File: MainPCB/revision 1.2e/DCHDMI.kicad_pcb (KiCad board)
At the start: 4 copper layers, 66.6 x 51.3 mm, 108 parts, among them CON1 3-1775333-2, CON2 2001-1-2-21-00-BK, U1 MCP1826S-1202E/DB, U2 MIC5219-2.5YM5-TR, U3 LP5907MFX-1.8/NOPB, U4 ADV7513, U5 664G-03LF, U6 10CL025, U7 MX25L1606EM1I-12G, U8 ESP-12E

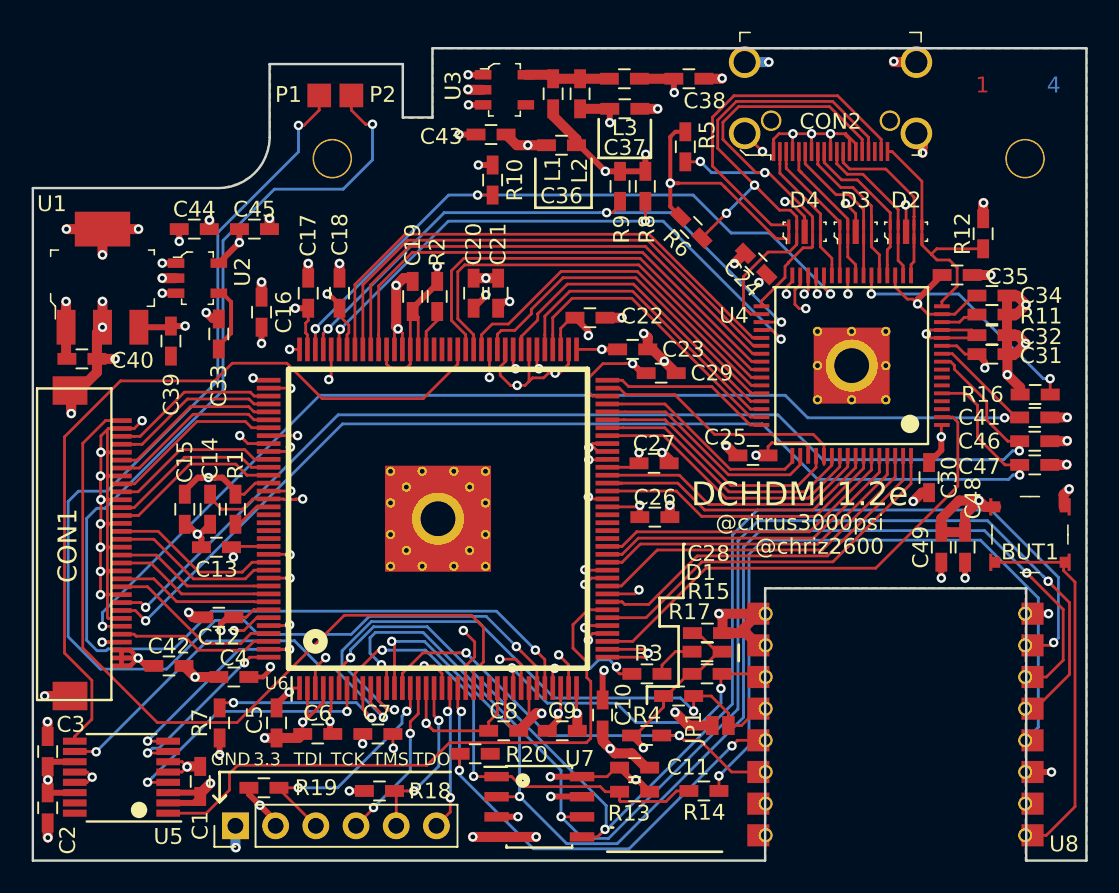
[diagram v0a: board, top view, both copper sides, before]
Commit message: Minor Update to Edge Cuts
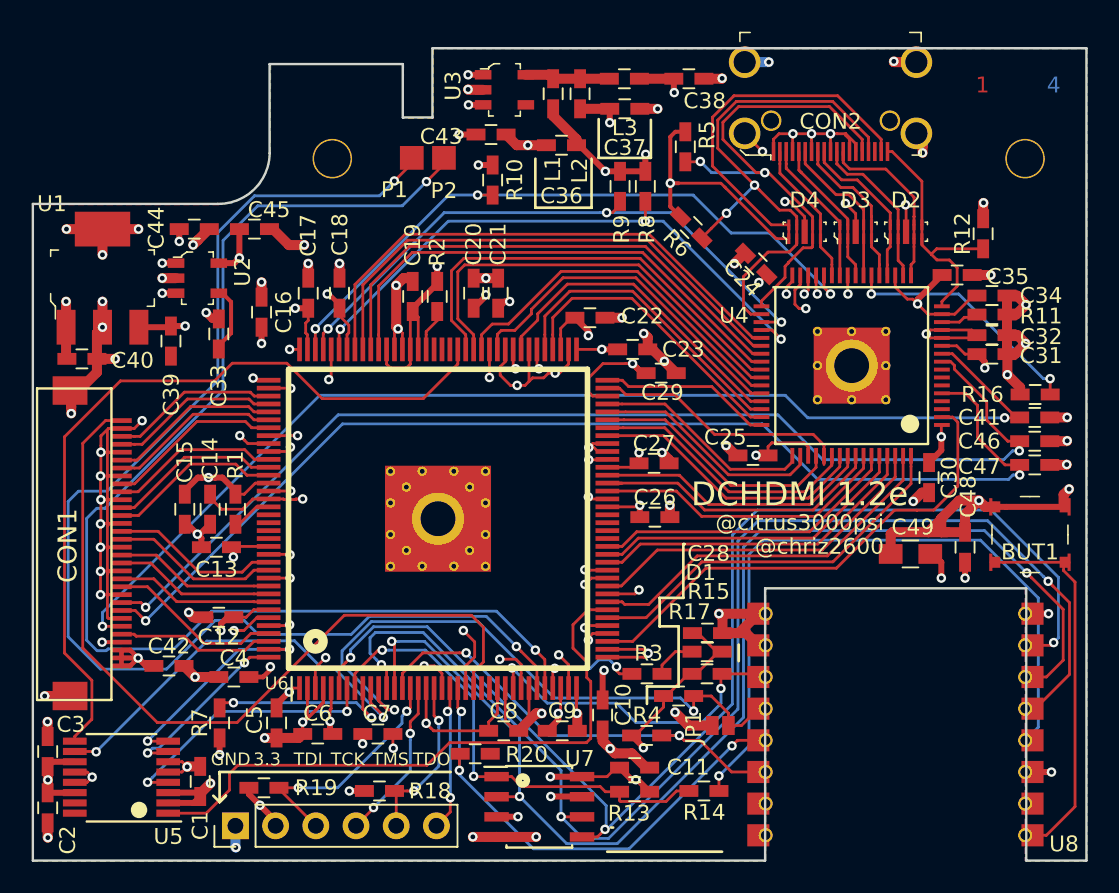
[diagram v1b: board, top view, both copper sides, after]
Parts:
- C49: footprint Capacitors_SMD:C_0603_HandSoldering -> Capacitors_SMD:C_0805_HandSoldering
- JP1: value (none) -> Jumper_NO_Small
- moved ? 7.05 mm to (148.0, 79.1)
- moved C49 2.00 mm to (177.4, 105.6), turned to 180 degrees
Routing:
- net GND: track 241.3 -> 254.1 mm
- net /PAD1: track 77.3 -> 80.2 mm
- net Net-(BUT1-Pad3): track 23.9 -> 24.6 mm
- net +1.2: track 181.5 -> 180.9 mm
- net +3V3: track 390.4 -> 389.8 mm
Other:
- outline, holes or cut-outs redrawn

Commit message: Edge Cuts Again
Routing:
- net /PAD1: track 80.2 -> 79.3 mm
- net /PAD2: track 78.8 -> 78.2 mm
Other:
- outline, holes or cut-outs redrawn
